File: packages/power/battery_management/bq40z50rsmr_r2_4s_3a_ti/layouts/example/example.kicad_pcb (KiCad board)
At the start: 2 copper layers, 29 parts

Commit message: Make package builds deterministic by wiring explicit local parts
The remaining packages now reference package-local concrete passives,
inductors, and other small parts directly instead of relying on generic
part-picker resolution. This aligns the source with the local
assets and removes the flaky live EasyEDA lookup path that was blocking
verification.

Constraint: Builds must not depend on unstable live part-picking when local package assets already exist
Constraint: Package-local parts remain the ownership boundary; no shared global part store was introduced
Rejected: Keep generic passives as the default style | repeated verification failures from upstream EasyEDA API instability
Rejected: Add ad hoc offline hacks around ato part-picking | weaker than making the package source deterministic
Confidence: high
Scope-risk: moderate
Reversibility: clean
Directive: For packages that already own generated local parts, instantiate those part modules directly and avoid generic passive declarations unless there is a strong reason not to
Tested:  passed for stm32g0b1kbu6_st, mcp2518fdt_e_sl_microchip, tcan3413ddfr_ti, raspberry_pi_hat_socket_zhouri, bq40z50rsmr_r2_4s_3a_ti, tps56637rpar_5v1_5a_ti, tps62933drlr_3v3_ti, bq25756rrvr_4s_2a_ti, tps2121ruxr_20v_4a_ti, and tps25730drefr_20v_3a_ti
Not-tested: Cross-package downstream integration beyond each package's default/example build
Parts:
- C1, C2, C3, C5, C6, C7, C8, C9: value 100nF ±10% -> (none)
- C4: value 2.2µF ±10% -> (none)
- R1, R3, R5: value 100kΩ ±1% -> (none)
- R10, R11, R12, R13, R6: value 10kΩ ±1% -> (none)
- R14, R15, R16, R17, R18, R2, R4, R8, R9: value 100Ω ±1% -> (none)
- R7: value 1mΩ ±1% -> (none)
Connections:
- net 10 renamed frontend-1-2
- net 11 renamed frontend-1-3
- net 12 renamed frontend-1-4
- net 13 renamed frontend-1-5
- net 4 renamed frontend-1
- net current_sense_filter-power-hv renamed srp_filtered
- net current_sense_filter-power-lv renamed srn_filtered
- net pack_bypass-power-hv renamed pack_filtered
- net pbi_hold_cap-power-hv renamed frontend-1-1
- net vc1_filter_cap-power-hv renamed frontend-1-8
- net vc2_filter_cap-power-hv renamed frontend-1-7
- net vc2_filter_cap-power-lv renamed tap_1
- net vc3_filter_cap-power-hv renamed frontend-1-6
- net vc3_filter_cap-power-lv renamed tap_2
- net vc4_filter_cap-power-hv renamed frontend-2-1
- net vc4_filter_cap-power-lv renamed tap_3
- net vcc_bypass-power-hv renamed vcc_filtered
- C1 pad 1: hv -> 1
- C1 pad 2: lv -> 2
- C3 pad 2: lv -> 2
- C4 pad 2: lv -> 2
- C5 pad 2: lv -> 2
- C9 pad 2: lv -> 2
- Q1 pad 1: hv -> 1
- Q1 pad 2: 2 -> frontend-2
- Q1 pad 3: pack-hv -> hv
- R1 pad 2: pack-hv -> hv
- R10 pad 2: lv -> 2
- R11 pad 2: lv -> 2
- R12 pad 2: lv -> 2
- R13 pad 2: lv -> 2
- R17 pad 1: hv -> 1
- R18 pad 1: hv -> 1
- R3 pad 1: 2 -> frontend-2
- R3 pad 2: hv -> 1
- R4 pad 2: 2 -> frontend-2
- R5 pad 1: hv -> 1
- R6 pad 1: pack-hv -> hv
- R7 pad 1: lv -> 2
- R7 pad 2: pack-lv -> lv
- R8 pad 1: lv -> 2
- R9 pad 1: pack-lv -> lv
- U1 pad 16: lv -> 2
- U1 pad 23: lv -> 2
- U1 pad 24: lv -> 2
- U1 pad 25: lv -> 2
- U1 pad 32: hv -> 1
- U1 pad 33: lv -> 2
- U1 pad 9: lv -> 2

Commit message: Make package schematics more readable and align passive choices with repo guidance
This pass improves the human-facing quality of the package library.
Explicit local capacitor/resistor parts now carry short descriptive
comments at the point of use, the MCP2518FD package swaps its 1uF bulk
capacitor to a 0603 part to match the current sizing rule, and several
packages add better net-name overrides for exposed and important internal
signals.

Constraint: Repo guidance now prefers explicit local parts and expects readable schematic net names
Constraint: Passive sizing should follow the current MLCC package rule unless a justified exception is needed
Rejected: Keep part instances comment-free | explicit local part names are not readable enough by themselves
Rejected: Leave the MCP2518FD 1uF bulk cap in 0402 | conflicts with the current 1uF-10uF 0603 guidance
Confidence: medium
Scope-risk: moderate
Reversibility: clean
Directive: When instantiating explicit local resistor/capacitor parts, include a short readable comment with the key value/package characteristics unless the name is already obviously human-readable
Tested:  passed for stm32g0b1kbu6_st, mcp2518fdt_e_sl_microchip, tcan3413ddfr_ti, raspberry_pi_hat_socket_zhouri, bq40z50rsmr_r2_4s_3a_ti, tps56637rpar_5v1_5a_ti, tps62933drlr_3v3_ti, bq25756rrvr_4s_2a_ti, tps2121ruxr_20v_4a_ti, and tps25730drefr_20v_3a_ti
Not-tested: Complete elimination of all internal autogenerated net labels in every package; some deep internal nets may still remain tool-driven
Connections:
- net 1 renamed CELL4
- net 2 renamed GND
- net fet_common renamed FET_COMMON
- net frontend-1 renamed CHG_GATE
- net frontend-1-1 renamed PBI_HOLD
- net frontend-1-2 renamed TS1_BIAS
- net frontend-1-3 renamed TS2_BIAS
- net frontend-1-4 renamed TS3_BIAS
- net frontend-1-5 renamed TS4_BIAS
- net frontend-1-6 renamed VC3_FILT
- net frontend-1-7 renamed VC2_FILT
- net frontend-1-8 renamed VC1_FILT
- net frontend-2 renamed DSG_GATE
- net frontend-2-1 renamed VC4_FILT
- net hv renamed PACK+
- net pack_filtered renamed PACK_FILT
- net srn_filtered renamed SRN_FILT
- net srp_filtered renamed SRP_FILT
- net tap_1 renamed CELL1
- net tap_2 renamed CELL2
- net tap_3 renamed CELL3
- net vcc_filtered renamed BAT_FILT

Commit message: Expose raw battery connections without forcing net overrides
The battery frontend no longer assigns override_net_name values, and it now
exports raw_battery alongside the protected pack so downstream designs can add
a connector or harness wiring at the package boundary. I also removed the
repository guidance that encouraged override-based naming and rebuilt the
checked-in layouts so their net metadata matches the source after the change.

Constraint: Package instances were breaking when internal net overrides propagated into downstream designs
Constraint: The protected pack API and 4S/3A electrical limits must remain intact
Rejected: Keep pack-only exposure and require downstream forks | blocks connector integration at the package boundary
Rejected: Leave checked-in layouts on the old net names | creates source/layout drift after rebuilds
Confidence: high
Scope-risk: moderate
Reversibility: clean
Directive: Prefer explicit exported interfaces like `pack` and `raw_battery` over internal net-name overrides
Tested: `uv tool run --from atopile==0.15.4 ato --non-interactive build` in `packages/power/battery_management/bq40z50rsmr_r2_4s_3a_ti`
Not-tested: Integration of `raw_battery` with a concrete downstream battery connector package
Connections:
- net BAT_FILT renamed vcc_filtered
- net CELL1 renamed tap_1
- net CELL2 renamed tap_2
- net CELL3 renamed tap_3
- net CELL4 renamed hv
- net CHG_GATE renamed 1
- net DSG_GATE renamed 2
- net FET_COMMON renamed fet_common
- net PACK+ renamed pack-hv
- net PACK_FILT renamed pack_filtered
- net PBI_HOLD renamed frontend-1
- net SRN_FILT renamed srn_filtered
- net SRP_FILT renamed srp_filtered
- net TS1_BIAS renamed frontend-1-1
- net TS2_BIAS renamed frontend-1-2
- net TS3_BIAS renamed frontend-1-3
- net TS4_BIAS renamed frontend-1-4
- net VC1_FILT renamed frontend-1-7
- net VC2_FILT renamed frontend-1-6
- net VC3_FILT renamed frontend-1-5
- net VC4_FILT renamed frontend-2
- C1 pad 2: GND -> lv
- C3 pad 2: GND -> lv
- C4 pad 2: GND -> lv
- C5 pad 2: GND -> lv
- C9 pad 2: GND -> lv
- R10 pad 2: GND -> lv
- R11 pad 2: GND -> lv
- R12 pad 2: GND -> lv
- R13 pad 2: GND -> lv
- R7 pad 1: GND -> lv
- R7 pad 2: lv -> pack-lv
- R8 pad 1: GND -> lv
- R9 pad 1: lv -> pack-lv
- U1 pad 16: GND -> lv
- U1 pad 23: GND -> lv
- U1 pad 24: GND -> lv
- U1 pad 25: GND -> lv
- U1 pad 33: GND -> lv
- U1 pad 9: GND -> lv

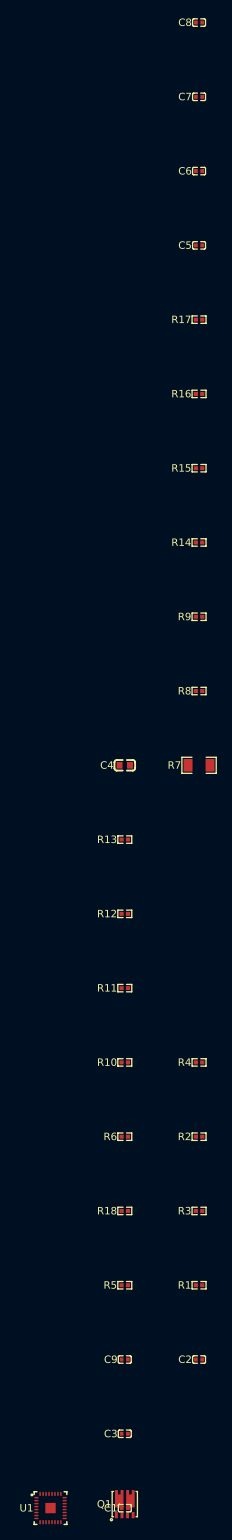
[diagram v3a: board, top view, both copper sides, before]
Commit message: Align the BQ40Z50 frontend with TI's recommended sense filtering
The cell-tap, SMBus, unused-pin, and PTC wiring had drifted from the TI
reference guidance. This updates the package so VC filtering happens on the
IC side of the 100 Ω resistors, unused TS/DISP pins are grounded, SMBus gets
series damping, unnecessary bypass caps are removed, and the PTC safety path
uses a concrete 0402 Murata part.

Constraint: Must keep the package reusable, deterministic, and sourced from LCSC parts already compatible with Atopile
Constraint: Verification must use ato in the changed package directory
Rejected: Keep TS pull-down resistors for unused inputs | datasheet guidance prefers direct VSS ties in this case
Rejected: Leave PTC unimplemented | user explicitly requested a concrete safety thermistor path
Confidence: medium
Scope-risk: moderate
Reversibility: clean
Directive: Re-check BQ40Z50 data-flash temperature and permanent-fail settings before changing the chosen PTC trip part or threshold assumptions
Tested:  in packages/power/battery_management/bq40z50rsmr_r2_4s_3a_ti (default and example)
Not-tested: Bench-level thermal trip behavior and SMBus signal integrity on hardware
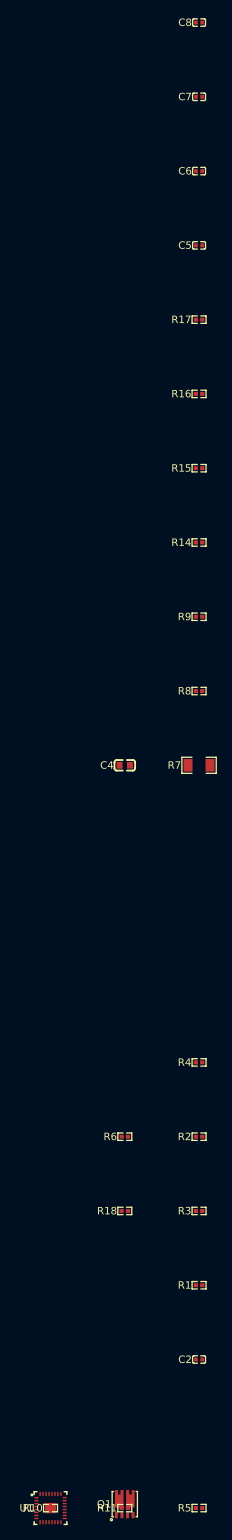
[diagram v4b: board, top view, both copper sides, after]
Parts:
- removed C1, C3, C9: , Murata_Electronics_GRM155R71H104KE14D:C0402
- removed R12, R13: , YAGEO_RC0402FR_0710KL:R0402
- R10, R11: footprint YAGEO_RC0402FR_0710KL:R0402 -> YAGEO_RC0402FR_07100RL:R0402
- R5: footprint YAGEO_RC0402FR_07100KL:R0402 -> Murata_Electronics_PRF15BB103RB6RC:R0402
- moved R11 70.0 mm to (10.0, 0.00)
- moved R10 60.8 mm to (0.00, 0.00)
- moved R5 31.6 mm to (20.0, 0.00)
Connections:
- net frontend-2 renamed vc4_filtered
- C4 pad 2: lv -> raw_battery-lv
- C5 pad 1: frontend-1-7 -> vc1_filtered
- C5 pad 2: lv -> raw_battery-lv
- C6 pad 1: frontend-1-6 -> vc2_filtered
- C6 pad 2: tap_1 -> vc1_filtered
- C7 pad 1: frontend-1-5 -> vc3_filtered
- C7 pad 2: tap_2 -> vc2_filtered
- C8 pad 2: tap_3 -> vc3_filtered
- Q1 pad 1: hv -> raw_battery-hv
- Q1 pad 3: pack-hv -> hv
- R1 pad 2: pack-hv -> hv
- R10 pad 1: frontend-1-1 -> SCL
- R10 pad 2: lv -> SMBC
- R11 pad 1: frontend-1-2 -> SDA
- R11 pad 2: lv -> SMBD
- R14 pad 2: frontend-1-7 -> vc1_filtered
- R15 pad 2: frontend-1-6 -> vc2_filtered
- R16 pad 2: frontend-1-5 -> vc3_filtered
- R17 pad 1: hv -> raw_battery-hv
- R18 pad 1: hv -> raw_battery-hv
- R3 pad 2: hv -> raw_battery-hv
- R5 pad 1: hv -> PTC
- R5 pad 2: nDISP -> raw_battery-hv
- R6 pad 1: pack-hv -> hv
- R7 pad 1: lv -> raw_battery-lv
- R7 pad 2: pack-lv -> lv
- R8 pad 1: lv -> raw_battery-lv
- R9 pad 1: pack-lv -> lv
- U1 pad 10: frontend-1-1 -> raw_battery-lv
- U1 pad 11: frontend-1-2 -> raw_battery-lv
- U1 pad 12: frontend-1-3 -> raw_battery-lv
- U1 pad 13: frontend-1-4 -> raw_battery-lv
- U1 pad 16: lv -> raw_battery-lv
- U1 pad 17: nDISP -> raw_battery-lv
- U1 pad 18: SDA -> SMBD
- U1 pad 19: SCL -> SMBC
- U1 pad 23: lv -> PTC
- U1 pad 24: lv -> raw_battery-hv
- U1 pad 25: lv -> raw_battery-lv
- U1 pad 3: frontend-1-5 -> vc3_filtered
- U1 pad 32: hv -> raw_battery-hv
- U1 pad 33: lv -> raw_battery-lv
- U1 pad 4: frontend-1-6 -> vc2_filtered
- U1 pad 5: frontend-1-7 -> vc1_filtered
- U1 pad 9: lv -> raw_battery-lv

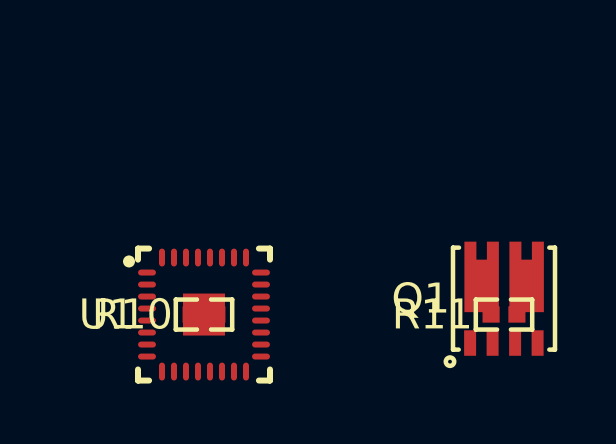
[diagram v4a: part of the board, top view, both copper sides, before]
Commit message: Filter the BQ40Z50 PTC input against switching noise
The new FET safety PTC path benefits from a local filter capacitor so the gauge
sees a cleaner temperature-protection signal instead of raw switching noise from
the pack side. This adds the requested 100 nF capacitor from PTC to BAT using
an existing package-local Murata MLCC.

Constraint: Must preserve the existing deterministic package-local part set where possible
Constraint: Verification must be done with ato in the changed package directory
Rejected: Add a new capacitor value/package just for the PTC node | existing 100 nF 0402 Murata part already fits the request
Rejected: Leave the PTC input unfiltered | user explicitly requested a filter capacitor
Confidence: high
Scope-risk: narrow
Reversibility: clean
Directive: Keep the PTC filter referenced to BAT unless the underlying TI protection network is re-derived from datasheet guidance
Tested:  in packages/power/battery_management/bq40z50rsmr_r2_4s_3a_ti (default and example)
Not-tested: Hardware-level noise immunity and trip response around the PTC input
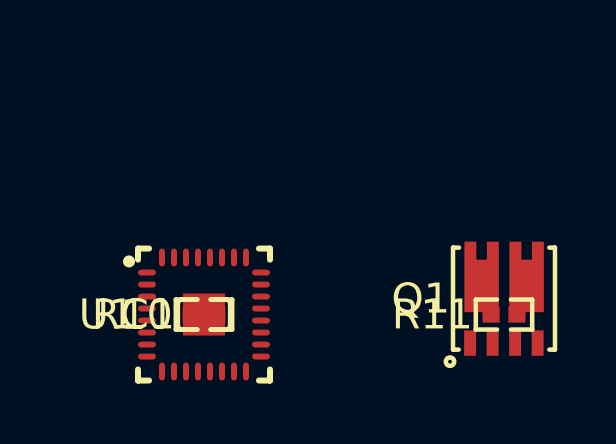
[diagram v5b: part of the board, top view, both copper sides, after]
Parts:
- added C1: , Murata_Electronics_GRM155R71E104KE14D:C0402, F.Cu at (0.00, 0.00)
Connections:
- C4 pad 1: frontend-1 -> frontend-1-1
- R5 pad 1: PTC -> frontend-1
- U1 pad 1: frontend-1 -> frontend-1-1
- U1 pad 23: PTC -> frontend-1
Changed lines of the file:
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@@
 	(net 44 "CHG")
 	(net 45 "pack_filtered")
-	(net 47 "frontend-1")
+	(net 47 "frontend-1-1")
 	(net 49 "hv")
 	(net 50 "fet_common")
@@
 	(net 2 "raw_battery-hv")
 	(net 3 "SMBD")
-	(net 4 "PTC")
 	(net 5 "SCL")
 	(net 6 "SMBC")
@@
 	(net 10 "vc3_filtered")
 	(net 11 "vc2_filtered")
+	(net 12 "frontend-1")
 	(footprint "Texas_Instruments_BQ40Z50RSMR_R2:VQFN-32_L4.0-W4.0-P0.40-TL-EP1.4_2"
 		(layer "F.Cu")
@@
 			(size 0.6 0.2)
 			(layers "F.Cu" "F.Paste" "F.Mask")
-			(net 4 "PTC")
+			(net 12 "frontend-1")
 		)
 		(pad "22" smd oval
@@
 			(size 0.6 0.2)
 			(layers "F.Cu" "F.Paste" "F.Mask")
-			(net 47 "frontend-1")
+			(net 47 "frontend-1-1")
 		)
 		(pad "33" smd rect
@@
 			(size 0.8 0.9)
 			(layers "F.Cu" "F.Paste" "F.Mask")
-			(net 47 "frontend-1")
+			(net 47 "frontend-1-1")
 		)
 		(embedded_fonts no)
@@
 			(size 0.57 0.54)
 			(layers "F.Cu" "F.Paste" "F.Mask")
-			(net 4 "PTC")
+			(net 12 "frontend-1")
 		)
 		(embedded_fonts no)
@@
 		)
 	)
+	(footprint "Murata_Electronics_GRM155R71E104KE14D:C0402"
+		(layer "F.Cu")
+		(at 0 0 0)
+		(property "Reference" "C1"
+			(at -0.97 0 0)
+			(layer "F.SilkS")
+			(effects
+				(font
+					(size 1 1)
+					(thickness 0.15)
+				)
+				(justify right)
+			)
+		)
+		(property "Value" ""
+			(at 0 4)
+			(layer "F.Fab")
+			(effects
+				(font
+					(size 1 1)
+					(thickness 0.15)
+				)
+			)
+		)
+		(property "LCSC" "C77014"
+			(at 0 0 0)
+			(layer "User.9")
+			(hide yes)
+		)
+		(property "Manufacturer" "Murata Electronics"
+			(at 0 0 0)
+			(layer "User.9")
+			(hide yes)
+		)
+		(property "Partnumber" "GRM155R71E104KE14D"
+			(at 0 0 0)
+			(layer "User.9")
+			(hide yes)
+		)
+		(property "Datasheet" "https://www.lcsc.com/datasheet/lcsc_datasheet_1811081616_Murata-Electronics-GRM155R71E104KE14D_C77014.pdf"
+			(at 0 0 0)
+			(layer "User.9")
+			(hide yes)
+		)
+		(property "atopile_address" "frontend.fet_safety_ptc_filter"
+			(at 0 0 0)
+			(layer "User.9")
+			(hide yes)
+		)
+		(property "atopile_subaddresses" "[layouts/default/default.kicad_pcb:fet_safety_ptc_filter]"
+			(at 0 0 0)
+			(layer "User.9")
+			(hide yes)
+		)
+		(property "lcsc_id" "C77014"
+			(at 0 0 0)
+			(layer "User.9")
+			(hide yes)
+		)
+		(attr smd)
+		(fp_line
+			(start -0.72 -0.5)
+			(end -0.22 -0.5)
+			(stroke
+				(width 0.15)
+				(type solid)
+			)
+			(layer "F.SilkS")
+			(layers "F.SilkS")
+			(locked no)
+		)
+		(fp_line
+			(start -0.87 0.35)
+			(end -0.87 -0.35)
+			(stroke
+				(width 0.15)
+				(type solid)
+			)
+			(layer "F.SilkS")
+			(layers "F.SilkS")
+			(locked no)
+		)
+		(fp_line
+			(start -0.22 0.5)
+			(end -0.72 0.5)
+			(stroke
+				(width 0.15)
+				(type solid)
+			)
+			(layer "F.SilkS")
+			(layers "F.SilkS")
+			(locked no)
+		)
+		(fp_line
+			(start 0.72 0.5)
+			(end 0.22 0.5)
+			(stroke
+				(width 0.15)
+				(type solid)
+			)
+			(layer "F.SilkS")
+			(layers "F.SilkS")
+			(locked no)
+		)
+		(fp_line
+			(start 0.22 -0.5)
+			(end 0.72 -0.5)
+			(stroke
+				(width 0.15)
+				(type solid)
+			)
+			(layer "F.SilkS")
+			(layers "F.SilkS")
+			(locked no)
+		)
+		(fp_line
+			(start 0.87 -0.35)
+			(end 0.87 0.35)
+			(stroke
+				(width 0.15)
+				(type solid)
+			)
+			(layer "F.SilkS")
+			(layers "F.SilkS")
+			(locked no)
+		)
+		(fp_arc
+			(start 0.87 -0.35)
+			(mid 0.826066 -0.456066)
+			(end 0.72 -0.5)
+			(stroke
+				(width 0.15)
+				(type solid)
+			)
+			(layer "F.SilkS")
+			(locked no)
+		)
+		(fp_arc
+			(start 0.72 0.5)
+			(mid 0.826066 0.456066)
+			(end 0.87 0.35)
+			(stroke
+				(width 0.15)
+				(type solid)
+			)
+			(layer "F.SilkS")
+			(locked no)
+		)
+		(fp_arc
+			(start -0.87 0.35)
+			(mid -0.826066 0.456066)
+			(end -0.72 0.5)
+			(stroke
+				(width 0.15)
+				(type solid)
+			)
+			(layer "F.SilkS")
+			(locked no)
+		)
+		(fp_arc
+			(start -0.72 -0.5)
+			(mid -0.826066 -0.456066)
+			(end -0.87 -0.35)
+			(stroke
+				(width 0.15)
+				(type solid)
+			)
+			(layer "F.SilkS")
+			(locked no)
+		)
+		(fp_circle
+			(center -0.5 0.25)
+			(end -0.47 0.25)
+			(stroke
+				(width 0.06)
+				(type solid)
+			)
+			(layer "F.Fab")
+			(locked no)
+		)
+		(pad "2" smd rect
+			(at 0.42 0 0)
+			(size 0.5 0.54)
+			(layers "F.Cu" "F.Paste" "F.Mask")
+			(net 2 "raw_battery-hv")
+		)
+		(pad "1" smd rect
+			(at -0.42 0 0)
+			(size 0.5 0.54)
+			(layers "F.Cu" "F.Paste" "F.Mask")
+			(net 12 "frontend-1")
+		)
+		(embedded_fonts no)
+		(model "${KIPRJMOD}/../../parts/Murata_Electronics_GRM155R71E104KE14D/C0402_L1.0-W0.5-H0.5.step"
+			(offset
+				(xyz 0 0 -0)
+			)
+			(scale
+				(xyz 1 1 1)
+			)
+			(rotate
+				(xyz 0 0 0)
+			)
+		)
+	)
 	(group "frontend"
 		(locked no)
@@
 			"9c0a2dce-0dee-4cd0-afa8-64574642524b" "9e6fc5f1-8bec-4b98-99dd-7c304642524b"
 			"a5fbdd3e-2a5e-4a89-acc9-f3424642524b" "a65df30b-2a15-4496-80b0-201e4642524b"
-			"bc1297fa-d3e8-45a6-8ff1-a8d64642524b" "ca30d0d8-e686-49a6-8ef0-a8e44642524b"
-			"cb8c4c7d-7b8b-4eac-8605-a9d14642524b" "cdb63e26-ae87-45bc-bbce-f99d4642524b"
-			"cdf4ff9e-c0ec-47e4-9cc9-bfcf4642524b" "e706bfb8-87fd-4019-80f6-82544642524b"
-			"e90448db-dad0-407d-8f4b-b6724642524b" "f16edb1e-230d-4a14-a522-1bca4642524b"
-			"f2f45ab2-37ea-4f17-a6c4-f7994642524b" "fcd1ef26-9636-42ba-84ab-aa474642524b"
+			"b1ce6c9a-0832-42e4-ab85-43174642524b" "bc1297fa-d3e8-45a6-8ff1-a8d64642524b"
+			"ca30d0d8-e686-49a6-8ef0-a8e44642524b" "cb8c4c7d-7b8b-4eac-8605-a9d14642524b"
+			"cdb63e26-ae87-45bc-bbce-f99d4642524b" "cdf4ff9e-c0ec-47e4-9cc9-bfcf4642524b"
+			"e706bfb8-87fd-4019-80f6-82544642524b" "e90448db-dad0-407d-8f4b-b6724642524b"
+			"f16edb1e-230d-4a14-a522-1bca4642524b" "f2f45ab2-37ea-4f17-a6c4-f7994642524b"
+			"fcd1ef26-9636-42ba-84ab-aa474642524b"
 		)
 	)
